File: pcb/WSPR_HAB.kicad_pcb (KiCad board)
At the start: 2 copper layers, 55 x 108.8 mm, 23 parts, among them J1 DC in, J2 Si5351, J3 LPF_input, J4 LPF_output, J5 EFHW_PRI, J6 EFHW_GND, J7 ANT_OUT, J8 ANT_GND, J9 EFHW_SEC, U1 5186, U2 7400

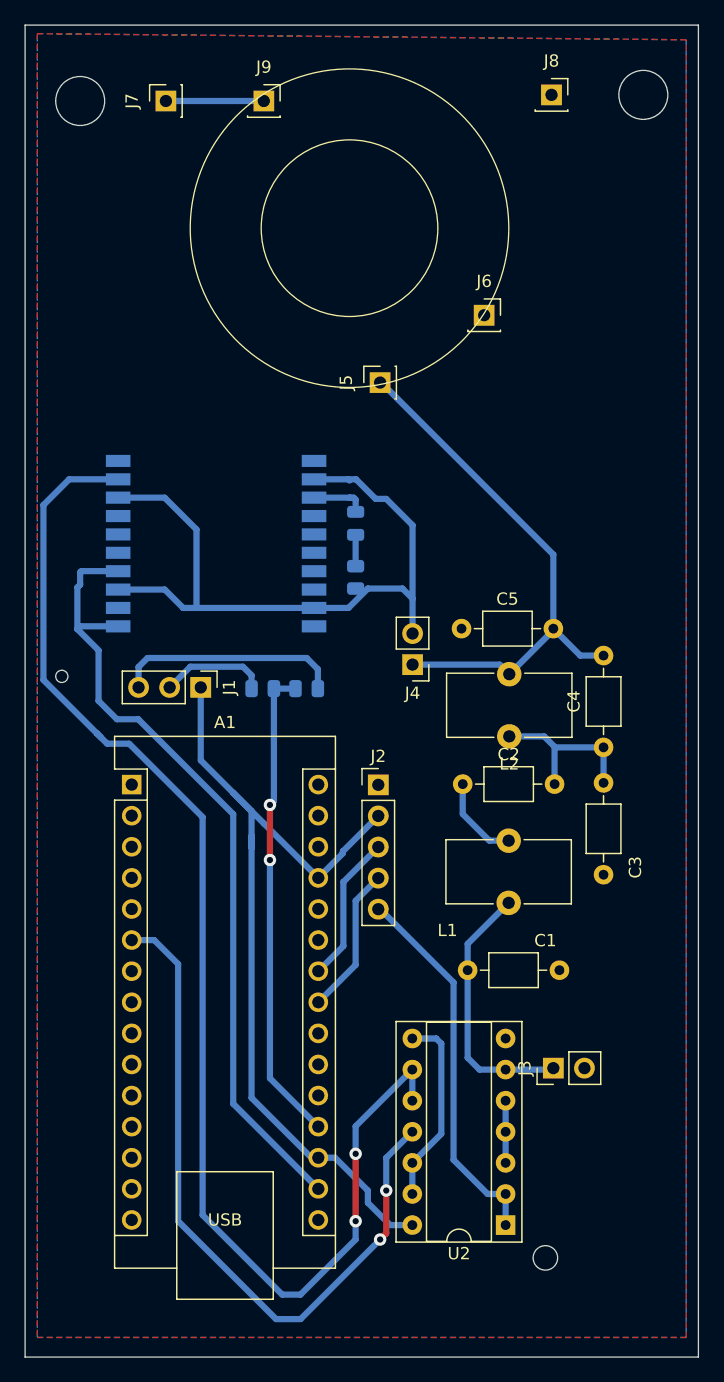
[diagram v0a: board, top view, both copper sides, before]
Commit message: added v1.2 PCB with fixes to the torroid size
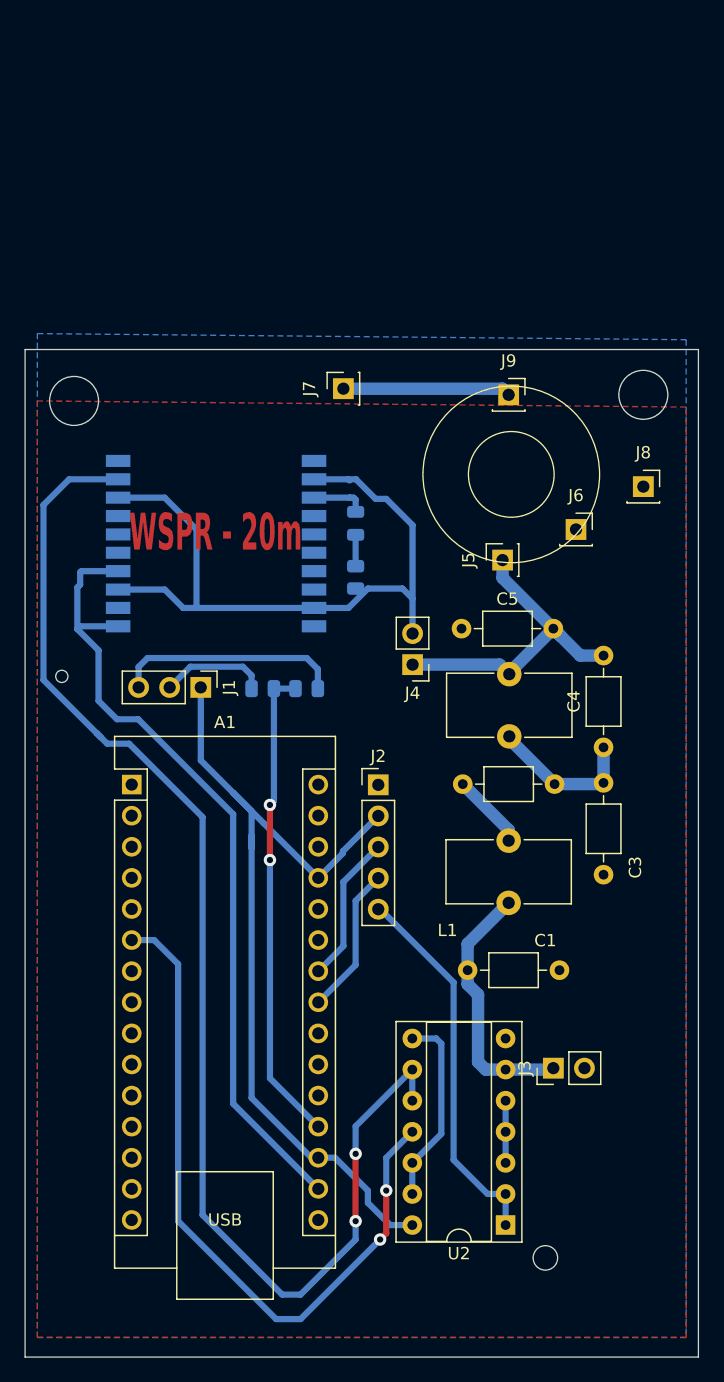
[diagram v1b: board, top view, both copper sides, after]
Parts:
- moved J8 32.9 mm to (106.5, 54.5)
- moved J9 31.2 mm to (95.5, 47.0)
- moved J7 27.6 mm to (82.0, 46.5)
- moved J6 19.0 mm to (101.0, 58.0)
- moved J5 17.6 mm to (95.0, 60.5)
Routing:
- net Net-(J4-Pin_1): track 44.4 -> 27.5 mm
- net Net-(J7-Pin_1): track 8.00 -> 13.7 mm
- net Net-(C2-Pad2): track 14.0 -> 12.4 mm
- net Net-(C2-Pad1): track 7.10 -> 6.17 mm
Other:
- board size 55 x 108.8 mm -> 55 x 82.3 mm
- board text added: "WSPR - 20m"
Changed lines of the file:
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@@
 	(footprint "Connector_PinSocket_2.54mm:PinSocket_1x01_P2.54mm_Vertical"
 		(layer "F.Cu")
-		(at 67.5 23 90)
+		(at 82 46.5 90)
 		(descr "Through hole straight socket strip, 1x01, 2.54mm pitch, single row (from Kicad 4.0.7), script generated")
 		(tags "Through hole socket strip THT 1x01 2.54mm single row")
@@
 			(at 0 -2.25 0)
 			(layer "F.SilkS")
+			(hide yes)
 			(effects
 				(font
@@
 	(footprint "Connector_PinSocket_2.54mm:PinSocket_1x01_P2.54mm_Vertical"
 		(layer "F.Cu")
-		(at 85 46 90)
+		(at 95 60.5 90)
 		(descr "Through hole straight socket strip, 1x01, 2.54mm pitch, single row (from Kicad 4.0.7), script generated")
 		(tags "Through hole socket strip THT 1x01 2.54mm single row")
@@
 		)
 		(property "Value" "EFHW_PRI"
-			(at 0 2.77 90)
+			(at -2.5 0.5 180)
 			(layer "F.Fab")
 			(effects
@@
 	(footprint "Connector_PinSocket_2.54mm:PinSocket_1x01_P2.54mm_Vertical"
 		(layer "F.Cu")
-		(at 99 22.5)
+		(at 106.5 54.5)
 		(descr "Through hole straight socket strip, 1x01, 2.54mm pitch, single row (from Kicad 4.0.7), script generated")
 		(tags "Through hole socket strip THT 1x01 2.54mm single row")
@@
 			(at 3.75 -2.42 0)
 			(layer "F.SilkS")
+			(hide yes)
 			(effects
 				(font
@@
 			(layer "F.Fab")
 		)
-		(fp_text user "${REFERENCE}"
-			(at 3.75 0 0)
-			(layer "F.Fab")
-			(effects
-				(font
-					(size 0.76 0.76)
-					(thickness 0.114)
-				)
-			)
-		)
 		(pad "1" thru_hole circle
 			(at 0 0)
@@
 	(footprint "Connector_PinSocket_2.54mm:PinSocket_1x01_P2.54mm_Vertical"
 		(layer "F.Cu")
-		(at 75.5 23)
+		(at 95.5 47)
 		(descr "Through hole straight socket strip, 1x01, 2.54mm pitch, single row (from Kicad 4.0.7), script generated")
 		(tags "Through hole socket strip THT 1x01 2.54mm single row")
@@
 	(footprint "Connector_PinSocket_2.54mm:PinSocket_1x01_P2.54mm_Vertical"
 		(layer "F.Cu")
-		(at 93.5 40.5)
+		(at 101 58)
 		(descr "Through hole straight socket strip, 1x01, 2.54mm pitch, single row (from Kicad 4.0.7), script generated")
 		(tags "Through hole socket strip THT 1x01 2.54mm single row")
@@
 		)
 		(property "Value" "EFHW_GND"
-			(at 0 2.77 0)
+			(at 3.5 0 90)
 			(layer "F.Fab")
 			(effects
@@
 	)
 	(gr_circle
-		(center 82.5 33.389236)
-		(end 73.3 42.589236)
+		(center 95.713875 53.5)
+		(end 99.213875 53.5)
 		(stroke
 			(width 0.1)
@@
 	)
 	(gr_circle
-		(center 82.5 33.389236)
-		(end 77.3 38.389236)
+		(center 95.713875 53.5)
+		(end 90.513875 58.5)
 		(stroke
 			(width 0.1)
@@
 	)
 	(gr_circle
-		(center 60.5 23)
-		(end 62.5 23)
+		(center 60 47.5)
+		(end 62 47.5)
 		(stroke
 			(width 0.05)
@@
 	)
 	(gr_circle
-		(center 106.5 22.5)
-		(end 108.5 22.5)
+		(center 106.5 47)
+		(end 108.5 47)
 		(stroke
 			(width 0.05)
@@
 	)
 	(gr_rect
-		(start 56 16.8)
+		(start 56 43.3)
 		(end 111 125.6)
 		(stroke
@@
 		(layer "Edge.Cuts")
 	)
+	(gr_text "WSPR - 20m"
+		(at 64.5 60 0)
+		(layer "F.Cu")
+		(effects
+			(font
+				(size 3 1.5)
+				(thickness 0.375)
+				(bold yes)
+			)
+			(justify left bottom)
+		)
+	)
 	(segment
 		(start 74.5 69.916)
@@
 	)
 	(segment
-		(start 94.77 69.04)
-		(end 95.55 69.82)
-		(width 0.508)
+		(start 95 61.95)
+		(end 95 60.5)
+		(width 1.016)
 		(layer "B.Cu")
 		(net 44)
 	)
 	(segment
-		(start 95.55 69.82)
-		(end 99.15 66.22)
-		(width 0.508)
+		(start 87.65 69.04)
+		(end 94.77 69.04)
+		(width 1.016)
 		(layer "B.Cu")
 		(net 44)
 	)
 	(segment
-		(start 99.15 60.05)
-		(end 85.1 46)
-		(width 0.508)
+		(start 95.55 69.7)
+		(end 99.15 66.1)
+		(width 1.016)
 		(layer "B.Cu")
 		(net 44)
 	)
 	(segment
-		(start 101.35 68.3)
-		(end 99.15 66.1)
+		(start 95.55 61.05)
+		(end 95 60.5)
 		(width 0.508)
 		(layer "B.Cu")
@@
 	)
 	(segment
-		(start 103.25 68.3)
-		(end 101.35 68.3)
-		(width 0.508)
+		(start 95.55 69.82)
+		(end 95.55 69.7)
+		(width 1.016)
 		(layer "B.Cu")
 		(net 44)
 	)
 	(segment
-		(start 99.15 66.1)
-		(end 99.15 60.05)
-		(width 0.508)
+		(start 99.775 66.725)
+		(end 95 61.95)
+		(width 1.016)
+		(layer "B.Cu")
+		(net 44)
+	)
+	(segment
+		(start 94.77 69.04)
+		(end 95.55 69.82)
+		(width 1.016)
+		(layer "B.Cu")
+		(net 44)
+	)
+	(segment
+		(start 99.775 66.725)
+		(end 99.15 66.1)
+		(width 1.016)
 		(layer "B.Cu")
 		(net 44)
@@
 	)
 	(segment
-		(start 87.65 69.04)
-		(end 94.77 69.04)
-		(width 0.508)
+		(start 103.25 68.3)
+		(end 101.35 68.3)
+		(width 1.016)
+		(layer "B.Cu")
+		(net 44)
+	)
+	(segment
+		(start 101.35 68.3)
+		(end 99.775 66.725)
+		(width 1.016)
 		(layer "B.Cu")
 		(net 44)
@@
 	)
 	(segment
-		(start 92.15 94)
-		(end 92.15 91.85)
-		(width 0.508)
+		(start 93.62 102.12)
+		(end 93 101.5)
+		(width 1.016)
 		(layer "B.Cu")
 		(net 49)
 	)
 	(segment
-		(start 92.15 91.85)
-		(end 95.5 88.5)
-		(width 0.508)
+		(start 93 96)
+		(end 92.15 95.15)
+		(width 1.016)
 		(layer "B.Cu")
 		(net 49)
 	)
 	(segment
-		(start 92.15 94)
-		(end 92.15 101.15)
-		(width 0.508)
+		(start 92.15 95.15)
+		(end 92.15 94)
+		(width 1.016)
 		(layer "B.Cu")
 		(net 49)
 	)
 	(segment
-		(start 93.12 102.12)
-		(end 95.25 102.12)
-		(width 0.508)
+		(start 95.25 102.12)
+		(end 93.62 102.12)
+		(width 1.016)
 		(layer "B.Cu")
 		(net 49)
 	)
 	(segment
-		(start 99.03 102.12)
-		(end 99.15 102)
-		(width 0.508)
+		(start 93 101.5)
+		(end 93 96)
+		(width 1.016)
 		(layer "B.Cu")
 		(net 49)
 	)
 	(segment
-		(start 92.15 101.15)
-		(end 93.12 102.12)
-		(width 0.508)
+		(start 95.25 102.12)
+		(end 99.03 102.12)
+		(width 1.016)
 		(layer "B.Cu")
 		(net 49)
 	)
 	(segment
-		(start 95.25 102.12)
-		(end 99.03 102.12)
-		(width 0.508)
+		(start 99.03 102.12)
+		(end 99.15 102)
+		(width 1.016)
 		(layer "B.Cu")
 		(net 49)
 	)
 	(segment
-		(start 91.75 78.8)
-		(end 91.75 81.25)
-		(width 0.508)
+		(start 92.15 94)
+		(end 92.15 91.85)
+		(width 1.016)
 		(layer "B.Cu")
-		(net 50)
+		(net 49)
 	)
 	(segment
-		(start 93.92 83.42)
-		(end 95.5 83.42)
-		(width 0.508)
+		(start 92.15 91.85)
+		(end 95.5 88.5)
+		(width 1.016)
+		(layer "B.Cu")
+		(net 49)
+	)
+	(segment
+		(start 95.5 82.55)
+		(end 91.75 78.8)
+		(width 1.016)
 		(layer "B.Cu")
 		(net 50)
 	)
 	(segment
-		(start 91.75 81.25)
-		(end 93.92 83.42)
-		(width 0.508)
+		(start 95.5 83.42)
+		(end 95.5 82.55)
+		(width 1.016)
 		(layer "B.Cu")
 		(net 50)
 	)
 	(segment
-		(start 95.55 74.9)
-		(end 98.4 74.9)
-		(width 0.508)
+		(start 99.25 78.8)
+		(end 103.15 78.8)
+		(width 1.016)
 		(layer "B.Cu")
 		(net 51)
 	)
 	(segment
-		(start 98.4 74.9)
-		(end 99.25 75.75)
-		(width 0.508)
+		(start 95.55 74.9)
+		(end 95.55 75.1)
+		(width 1.016)
 		(layer "B.Cu")
 		(net 51)
 	)
 	(segment
-		(start 103.25 75.8)
-		(end 99.3 75.8)
-		(width 0.508)
+		(start 95.55 75.1)
+		(end 99.25 78.8)
+		(width 1.016)
 		(layer "B.Cu")
 		(net 51)
 	)
 	(segment
-		(start 99.3 75.8)
-		(end 99.25 75.75)
-		(width 0.508)
+		(start 103.15 78.8)
+		(end 103.25 78.7)
+		(width 1.016)
 		(layer "B.Cu")
 		(net 51)
 	)
 	(segment
-		(start 99.25 75.75)
-		(end 99.25 78.8)
-		(width 0.508)
+		(start 103.25 75.8)
+		(end 103.25 78.7)
+		(width 1.016)
 		(layer "B.Cu")
 		(net 51)
 	)
 	(segment
-		(start 103.25 78.7)
-		(end 103.25 75.8)
-		(width 0.508)
+		(start 95 46.5)
+		(end 95.5 47)
+		(width 1.016)
 		(layer "B.Cu")
-		(net 51)
+		(net 52)
 	)
 	(segment
-		(start 67.5 23)
-		(end 75.5 23)
-		(width 0.508)
+		(start 82 46.5)
+		(end 95 46.5)
+		(width 1.016)
 		(layer "B.Cu")
 		(net 52)
 	)
 	(zone
+		(net 0)
+		(net_name "")
+		(layer "F.Cu")
+		(hatch edge 0.5)
+		(connect_pads
+			(clearance 0)
+		)
+		(min_thickness 0.25)
+		(filled_areas_thickness no)
+		(keepout
+			(tracks allowed)
+			(vias allowed)
+			(pads allowed)
+			(copperpour not_allowed)
+			(footprints allowed)
+		)
+		(fill
+			(thermal_gap 0.5)
+			(thermal_bridge_width 0.5)
+		)
+		(polygon
+			(pts
+				(xy 56.5 44) (xy 111 44) (xy 110.5 67) (xy 56.5 67)
+			)
+		)
+	)
+	(zone
 		(net 2)
 		(net_name "GND")
@@
 		(polygon
 			(pts
-				(xy 57 124) (xy 110 124) (xy 110 18) (xy 57 17.5)
+				(xy 57 124) (xy 110 124) (xy 110 48) (xy 57 47.5)
 			)
 		)
@@
 		(polygon
 			(pts
-				(xy 57 17.5) (xy 110 18) (xy 110 124) (xy 57 124)
+				(xy 57 42) (xy 110 42.5) (xy 110 124) (xy 57 124)
 			)
 		)
@@
 		(polygon
 			(pts
-				(xy 61 49) (xy 61 67) (xy 86 67) (xy 86 49)
+				(xy 61 50) (xy 61 67) (xy 86 67) (xy 86 50)
 			)
 		)

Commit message: added the Si5351 to the PCB
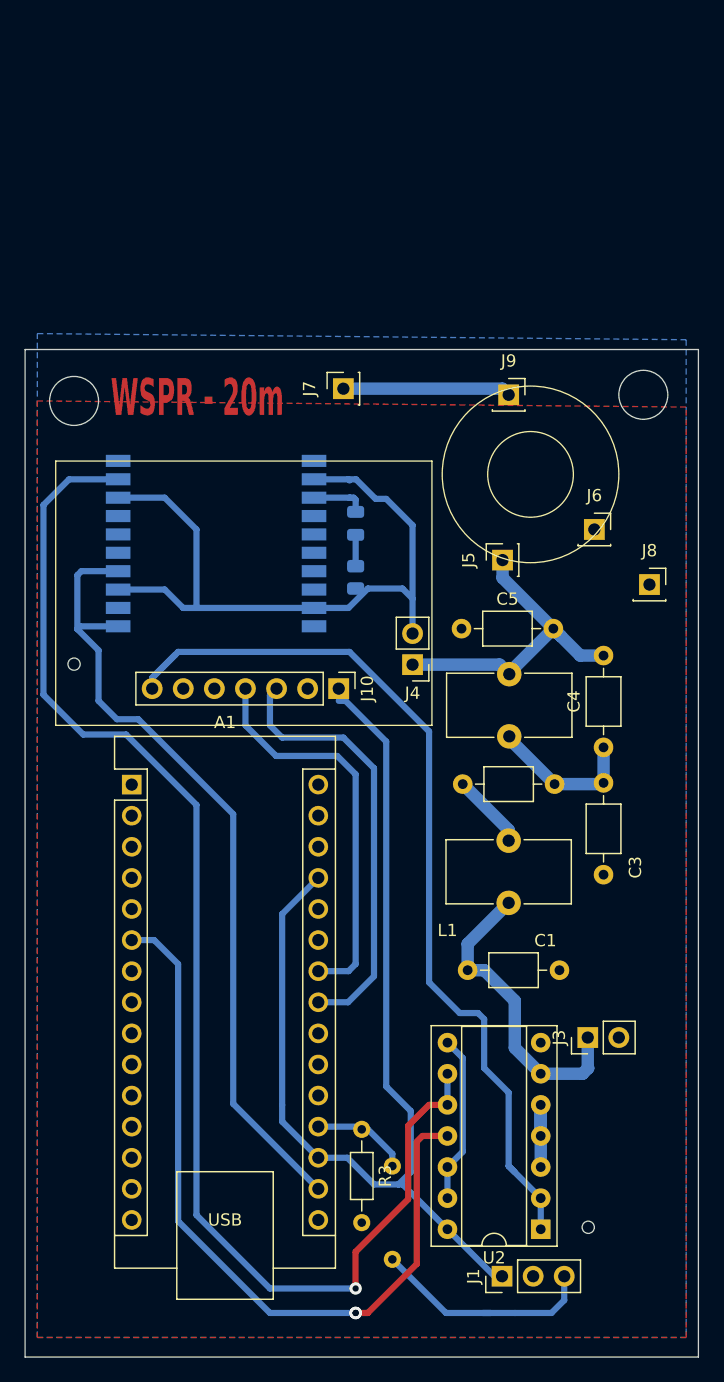
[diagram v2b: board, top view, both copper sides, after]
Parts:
- removed J2: Si5351, Connector_PinHeader_2.54mm:PinHeader_1x05_P2.54mm_Vertical
- added J10: Si5351, Connector_PinHeader_2.54mm:PinHeader_1x07_P2.54mm_Vertical, F.Cu at (81.6, 71.0)
- R2: footprint Resistor_SMD:R_0805_2012Metric -> Resistor_THT:R_Axial_DIN0204_L3.6mm_D1.6mm_P7.62mm_Horizontal
- R3: footprint Resistor_SMD:R_0805_2012Metric -> Resistor_THT:R_Axial_DIN0204_L3.6mm_D1.6mm_P7.62mm_Horizontal; moved to F.Cu
- moved J1 54.0 mm to (95.0, 119.0), turned to 90 degrees
- moved R2 47.1 mm to (86.0, 117.6), turned to 90 degrees
- moved R3 36.9 mm to (83.5, 107.0), turned to -90 degrees
- moved J8 8.02 mm to (107.0, 62.5)
- moved J3 3.76 mm to (102.0, 99.5)
- moved U2 2.89 mm to (98.1, 115.2)
- moved J6 1.50 mm to (102.5, 58.0)
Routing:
- net CLK0: track 31.1 -> 75.7 mm
- net V_measure: track 39.3 -> 7.97 mm, vias 2 -> 0
- net SDA: track 12.2 -> 35.6 mm
- net SCL: track 12.2 -> 32.4 mm
- net VCC: track 71.2 -> 87.6 mm
- net GND: track 66.9 -> 58.1 mm
- net GPS_tx: track 58.0 -> 62.6 mm
- net Net-(J3-Pin_1): track 21.2 -> 25.2 mm
- net Net-(U2-Pad3): track 5.08 -> 7.62 mm
- net Net-(U2-Pad12): track 15.8 -> 13.7 mm
- net Net-(U1-TX0): track 107.3 -> 109.2 mm, vias 2 -> 1
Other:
- outline, holes or cut-outs redrawn

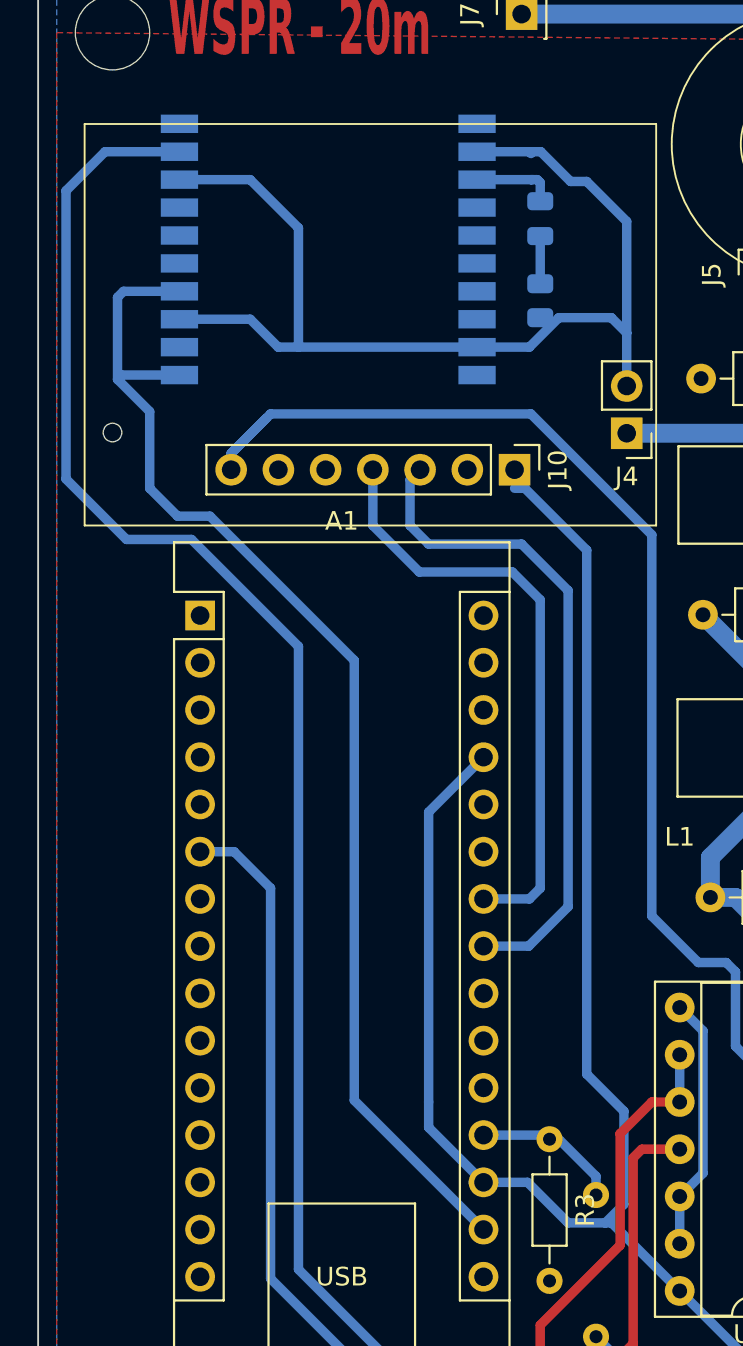
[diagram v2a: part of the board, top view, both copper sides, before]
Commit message: added a mosfet and extra pins to the gps
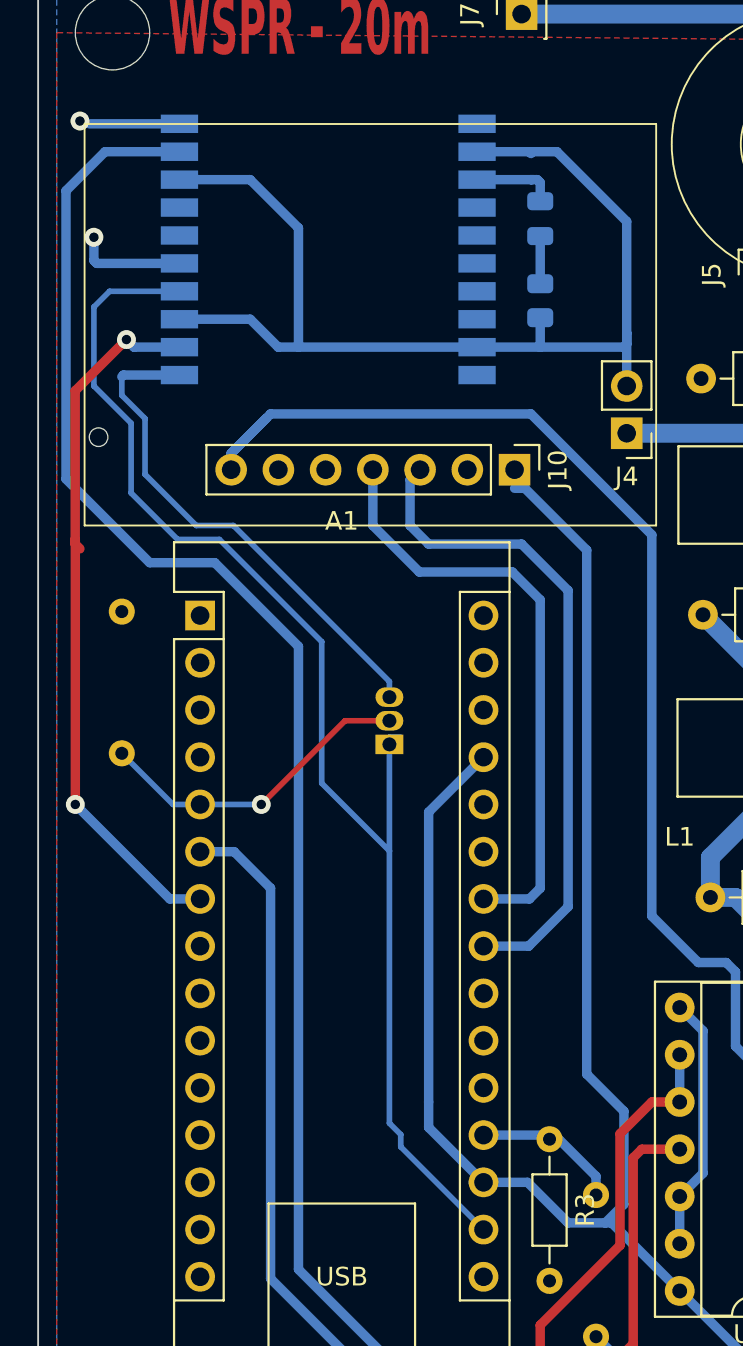
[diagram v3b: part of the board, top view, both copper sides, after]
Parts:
- added Q1: BS170, Package_TO_SOT_THT:TO-92_Inline, B.Cu at (74.9, 85.8)
- added R4: 10k, Resistor_THT:R_Axial_DIN0204_L3.6mm_D1.6mm_P7.62mm_Horizontal, B.Cu at (60.5, 86.2)
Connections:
- A1 pad 5: unconnected-(A1-D2-Pad5) -> GPS_cutoff
- A1 pad 7: unconnected-(A1-D4-Pad7) -> GPS_reset
- U1 pad 1: v3.3 -> GPS_Vcc
- U1 pad 2: unconnected-(U1-NRESET-Pad2) -> GPS_reset
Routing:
- net GPS_reset: track 0.00 -> 38.8 mm, vias 0 -> 2
- net GPS_Vcc: track 0.00 -> 27.5 mm
- net GPS_cutoff: track 0.00 -> 17.4 mm, vias 0 -> 1
- net unconnected-(U1-3D-FIX-Pad5): track 0.00 -> 5.91 mm, vias 0 -> 1
- net v3.3: track 66.2 -> 71.3 mm
- net unconnected-(U1-RX0-Pad10): track 0.00 -> 5.06 mm, vias 0 -> 1
- net GND: track 58.1 -> 59.4 mm
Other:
- outline, holes or cut-outs redrawn
